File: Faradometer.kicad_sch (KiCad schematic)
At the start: 20 parts, among them J101 Conn_01x02_Pin, J102 Conn_01x03_Pin, U101 TL072CP, U102 TL072CP

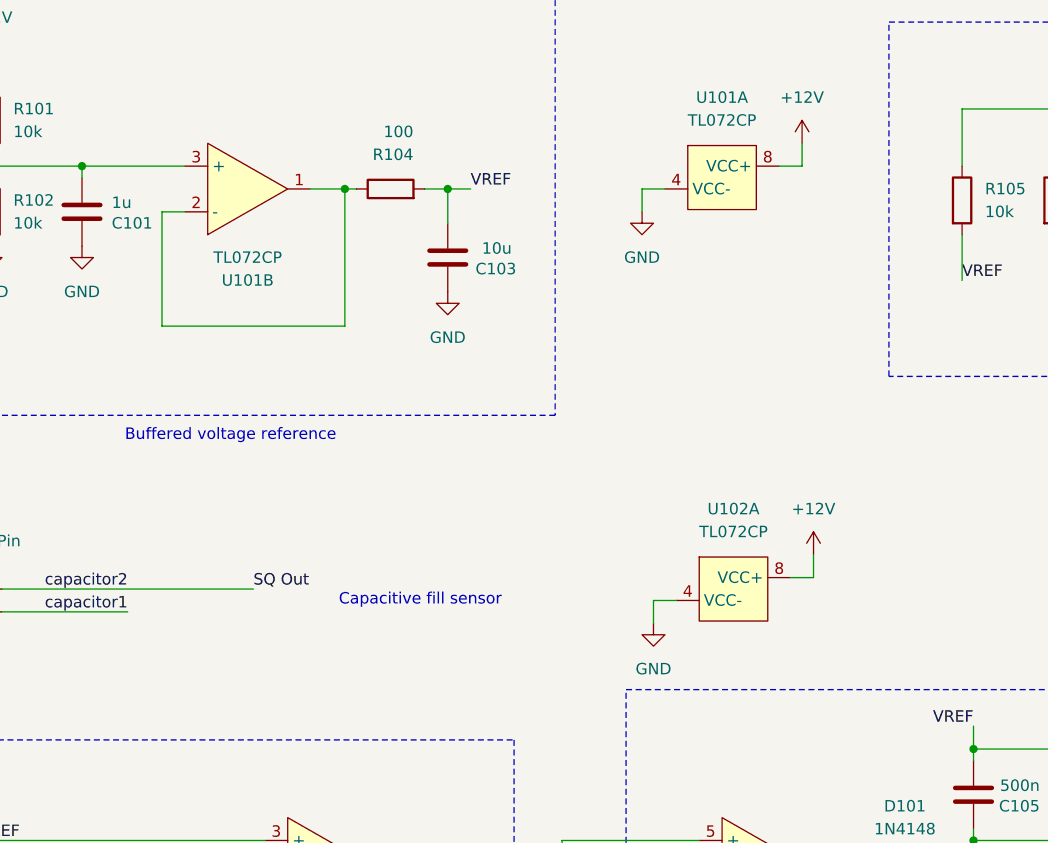
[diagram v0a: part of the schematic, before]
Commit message: Add .gitignore for KiCad junk files
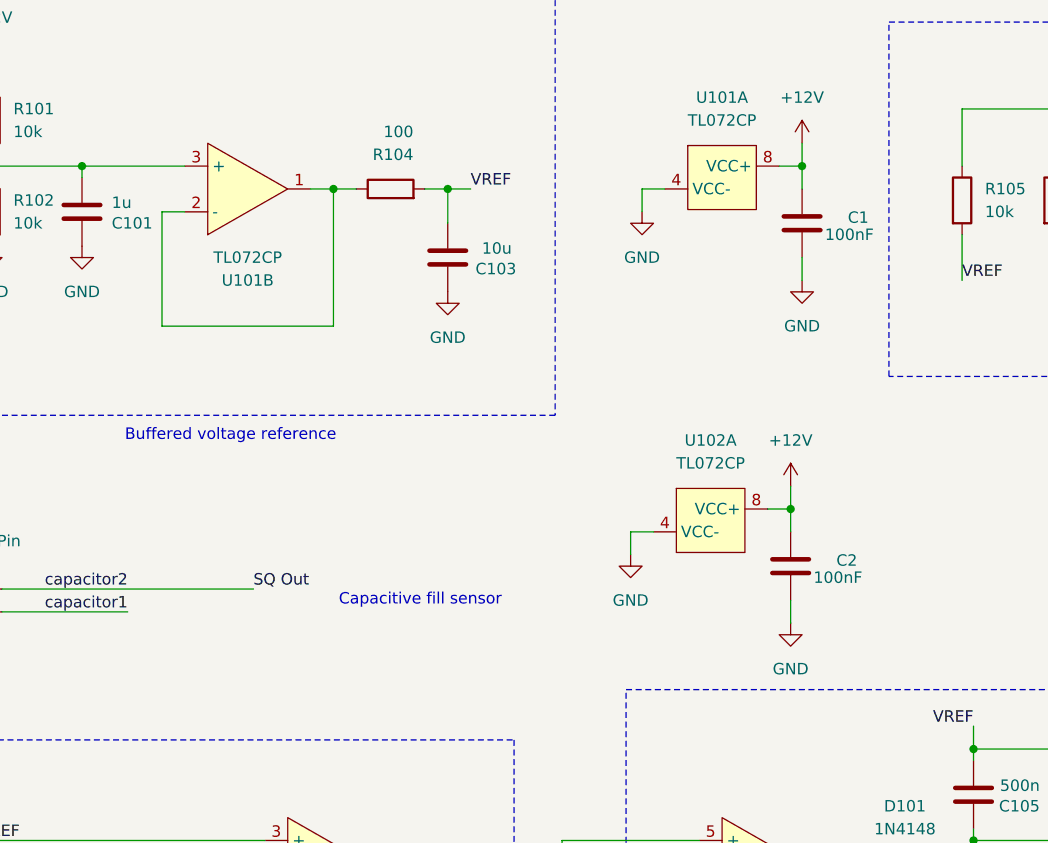
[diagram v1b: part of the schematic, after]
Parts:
- added C1, C2: 100nF, Capacitor_SMD:C_0805_2012Metric_Pad1.18x1.45mm_HandSolder, symbol Device:C
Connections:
- net +12V: now also C1.1, C2.1
- net GND: now also C1.2, C2.2
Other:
- moved on the sheet: U102A
